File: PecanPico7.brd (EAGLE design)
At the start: 34.2 x 50 mm, 161 parts, among them IC1 Si4464-B1B-FM, IC10 TC1185-1.8VCT713, IC11 TC1185-2.5VCT713, IC12 ADR380ARTZ, IC13 RF6886, IC14 ALM-GP003, IC2 Si4464-B1B-FM, IC3 BME280_BME280, IC4 UBLOX_MAX-6, IC5 STM32F429IIH6, IC7 SPV1040, IC8 TXC_7Z, IC9 TPS62260DRVT, Q1 AP2301, Q2 AP2301, Q3 AP2301, U1 USD-SOCKETUSD, U2 PAC1720-1-AIA-TR, X1 CAMERA_HEADER

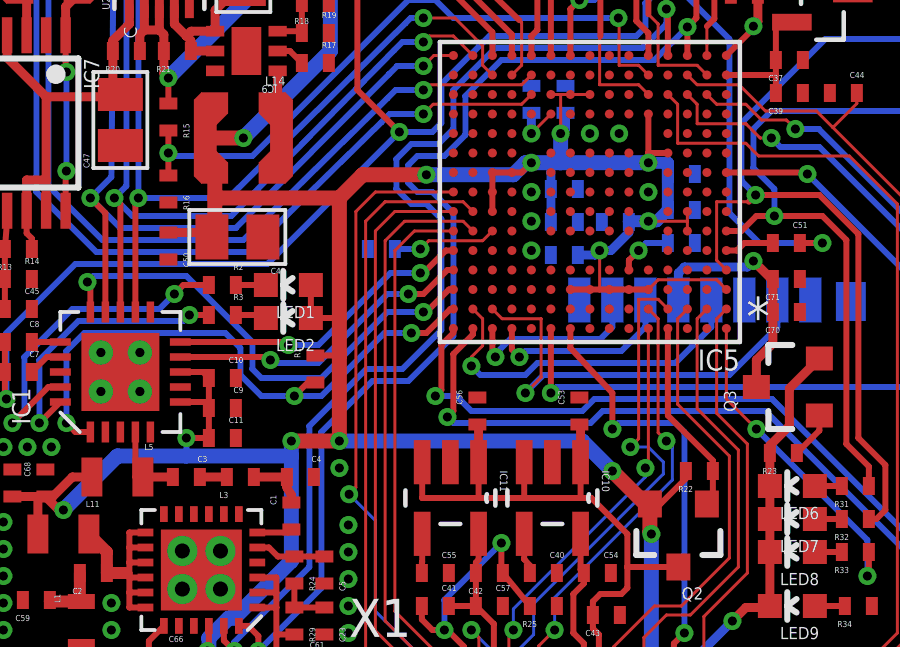
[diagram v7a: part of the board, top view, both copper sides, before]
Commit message: Moved parts around
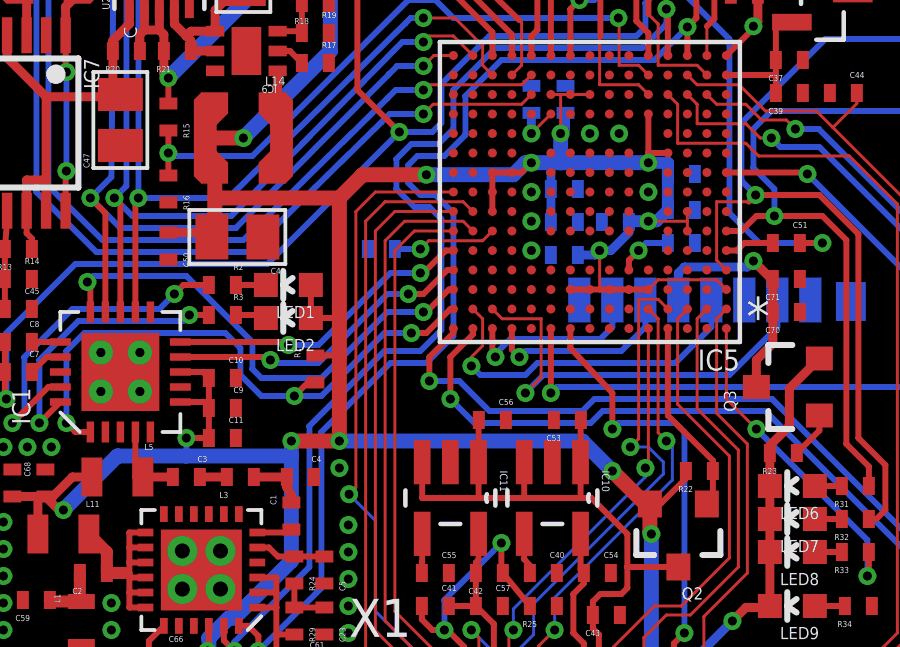
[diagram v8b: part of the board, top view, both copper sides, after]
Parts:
- moved C56 0.58 mm to (16.9, 14.5), turned to 180 degrees
- moved C53 0.50 mm to (19.4, 14.5), turned to 0 degrees
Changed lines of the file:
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@@
 </element>
 <element name="C40" library="PecanPico6" package="0402" value="470pF" x="18.6" y="9.4" rot="R180"/>
-<element name="C53" library="PecanPico6" package="0402" value="1uF" x="19.8" y="14.8" rot="R270"/>
+<element name="C53" library="PecanPico6" package="0402" value="1uF" x="19.4" y="14.5"/>
 <element name="C54" library="PecanPico6" package="0402" value="1uF" x="20.4" y="9.4" rot="R180"/>
 <element name="IC11" library="stm32f42x" package="SOT95P290X145-5N" value="TC1185-2.5VCT713" x="15.5" y="11.9" rot="R270">
@@
 </element>
 <element name="C55" library="PecanPico6" package="0402" value="470pF" x="15" y="9.4" rot="R180"/>
-<element name="C56" library="PecanPico6" package="0402" value="1uF" x="16.4" y="14.8" rot="R270"/>
+<element name="C56" library="PecanPico6" package="0402" value="1uF" x="16.9" y="14.5" rot="R180"/>
 <element name="C57" library="PecanPico6" package="0402" value="1uF" x="16.8" y="8.3" rot="R180"/>
 <element name="BATT" library="stm32f42x" package="LP-443440" value="LP-443440" x="17.1" y="20.1" rot="MR0"/>
@@
 <wire x1="23.7" y1="29.85" x2="24.85" y2="29.775" width="0" layer="19" extent="1-1"/>
 <wire x1="22.7" y1="29.85" x2="23.7" y2="29.85" width="0" layer="19" extent="1-1"/>
-<wire x1="19.8" y1="15.25" x2="19.5" y2="19.5" width="0" layer="19" extent="1-1"/>
-<wire x1="18.9" y1="13.0938" x2="19.8" y2="15.25" width="0" layer="19" extent="1-1"/>
-<wire x1="16.4" y1="15.25" x2="18.9" y2="13.0938" width="0" layer="19" extent="1-1"/>
-<wire x1="15.5" y1="13.0938" x2="16.4" y2="15.25" width="0" layer="19" extent="1-1"/>
+<wire x1="18.95" y1="14.5" x2="19.5" y2="19.5" width="0" layer="19" extent="1-1"/>
+<wire x1="18.9" y1="13.0938" x2="18.95" y2="14.5" width="0" layer="19" extent="1-1"/>
+<wire x1="17.35" y1="14.5" x2="18.9" y2="13.0938" width="0" layer="19" extent="1-1"/>
+<wire x1="15.5" y1="13.0938" x2="17.35" y2="14.5" width="0" layer="19" extent="1-1"/>
 <wire x1="19.05" y1="9.4" x2="18.9" y2="13.0938" width="0" layer="19" extent="1-1"/>
 <wire x1="19.05" y1="8.3" x2="19.05" y2="9.4" width="0" layer="19" extent="1-1"/>
@@
 <signal name="SWCLK">
 <contactref element="IC5" pad="A14"/>
-<via x="15.4" y="14.6" extent="1-16" drill="0.3"/>
+<via x="15.5" y="15.2" extent="1-16" drill="0.3"/>
 <wire x1="20.575" y1="14.8" x2="26" y2="14.8" width="0.2" layer="16"/>
 <wire x1="30.9" y1="9.9" x2="30.9" y2="5.84" width="0.2" layer="16"/>
-<wire x1="15.4" y1="14.6" x2="15.6" y2="14.4" width="0.2" layer="16"/>
-<wire x1="15.6" y1="14.4" x2="20.175" y2="14.4" width="0.2" layer="16"/>
+<wire x1="15.5" y1="15.2" x2="16.3" y2="14.4" width="0.2" layer="16"/>
+<wire x1="16.3" y1="14.4" x2="20.175" y2="14.4" width="0.2" layer="16"/>
 <wire x1="16.25" y1="17.55" x2="16.25" y2="17.35" width="0.2" layer="1"/>
-<wire x1="16.25" y1="17.35" x2="15.6" y2="16.7" width="0.2" layer="1"/>
-<wire x1="15.6" y1="16.7" x2="15.6" y2="14.8" width="0.2" layer="1"/>
-<wire x1="15.6" y1="14.8" x2="15.4" y2="14.6" width="0.2" layer="1"/>
+<wire x1="16.25" y1="17.35" x2="15.5" y2="16.6" width="0.2" layer="1"/>
+<wire x1="15.5" y1="16.6" x2="15.5" y2="15.2" width="0.2" layer="1"/>
 <wire x1="20.575" y1="14.8" x2="20.175" y2="14.4" width="0.2" layer="16"/>
 <contactref element="JP3" pad="2"/>
@@
 <signal name="SWDIO">
 <contactref element="IC5" pad="A15"/>
-<via x="15" y="15.3" extent="1-16" drill="0.3"/>
+<via x="14.8" y="15.8" extent="1-16" drill="0.3"/>
 <wire x1="20.3" y1="15.2" x2="26.22" y2="15.2" width="0.2" layer="16"/>
 <wire x1="19.9" y1="14.8" x2="20.3" y2="15.2" width="0.2" layer="16"/>
-<wire x1="15" y1="15.3" x2="15.7" y2="15.3" width="0.2" layer="16"/>
-<wire x1="15.7" y1="15.3" x2="16.2" y2="14.8" width="0.2" layer="16"/>
-<wire x1="16.2" y1="14.8" x2="19.9" y2="14.8" width="0.2" layer="16"/>
+<wire x1="14.8" y1="15.8" x2="15.8" y2="15.8" width="0.2" layer="16"/>
+<wire x1="15.8" y1="15.8" x2="16.8" y2="14.8" width="0.2" layer="16"/>
+<wire x1="16.8" y1="14.8" x2="19.9" y2="14.8" width="0.2" layer="16"/>
 <wire x1="15.6" y1="17.55" x2="15.6" y2="17.4" width="0.2" layer="1"/>
-<wire x1="15.6" y1="17.4" x2="15.2" y2="17" width="0.2" layer="1"/>
-<wire x1="15.2" y1="17" x2="15.2" y2="15.5" width="0.2" layer="1"/>
-<wire x1="15.2" y1="15.5" x2="15" y2="15.3" width="0.2" layer="1"/>
+<wire x1="15.6" y1="17.4" x2="14.8" y2="16.6" width="0.2" layer="1"/>
+<wire x1="14.8" y1="16.6" x2="14.8" y2="15.8" width="0.2" layer="1"/>
 <contactref element="JP3" pad="4"/>
 <wire x1="26.22" y1="15.2" x2="31.8" y2="9.6" width="0.2" layer="16"/>
@@
 <wire x1="8.3" y1="7.1" x2="10.8" y2="9.6" width="0.2" layer="16"/>
 <wire x1="10.8" y1="9.6" x2="10.8" y2="14.3" width="0.2" layer="16"/>
-<wire x1="10.8" y1="14.3" x2="12.7" y2="16.2" width="0.2" layer="16"/>
-<wire x1="12.7" y1="16.2" x2="13.9" y2="16.2" width="0.2" layer="16"/>
+<wire x1="10.8" y1="14.3" x2="13.3" y2="16.8" width="0.2" layer="16"/>
+<wire x1="13.3" y1="16.8" x2="14.5" y2="16.8" width="0.2" layer="16"/>
 <via x="22.7" y="28.2" extent="1-16" drill="0.3"/>
 <contactref element="IC5" pad="R4"/>
@@
 <wire x1="14.2" y1="23.7" x2="13.7" y2="23.2" width="0.2" layer="16"/>
 <wire x1="13.7" y1="23.2" x2="13.7" y2="22.2" width="0.2" layer="16"/>
-<wire x1="13.7" y1="22.2" x2="14.2" y2="21.7" width="0.2" layer="16"/>
-<wire x1="14.2" y1="21.7" x2="14.7" y2="21.7" width="0.2" layer="16"/>
-<wire x1="14.7" y1="21.7" x2="15.2" y2="21.2" width="0.2" layer="16"/>
+<wire x1="13.7" y1="22.2" x2="14.3" y2="21.6" width="0.2" layer="16"/>
+<wire x1="14.3" y1="21.6" x2="14.8" y2="21.6" width="0.2" layer="16"/>
+<wire x1="14.8" y1="21.6" x2="15.2" y2="21.2" width="0.2" layer="16"/>
 <wire x1="15.2" y1="21.2" x2="15.2" y2="17.5" width="0.2" layer="16"/>
-<wire x1="15.2" y1="17.5" x2="13.9" y2="16.2" width="0.2" layer="16"/>
+<wire x1="15.2" y1="17.5" x2="14.5" y2="16.8" width="0.2" layer="16"/>
 <contactref element="C72" pad="P$2"/>
 <wire x1="22.7" y1="28.2" x2="22.7" y2="28.95" width="0.2" layer="1"/>
@@
 <wire x1="9.1" y1="6.8" x2="11.2" y2="8.9" width="0.2" layer="16"/>
 <wire x1="11.2" y1="8.9" x2="11.2" y2="14.1" width="0.2" layer="16"/>
-<wire x1="11.2" y1="14.1" x2="12.9" y2="15.8" width="0.2" layer="16"/>
+<wire x1="11.2" y1="14.1" x2="13.5" y2="16.4" width="0.2" layer="16"/>
 <wire x1="9.1" y1="7.3" x2="9.1" y2="6.8" width="0.2" layer="1"/>
-<wire x1="12.9" y1="15.8" x2="14.1" y2="15.8" width="0.2" layer="16"/>
+<wire x1="13.5" y1="16.4" x2="14.7" y2="16.4" width="0.2" layer="16"/>
 <via x="23.4" y="27.6" extent="1-16" drill="0.3"/>
 <contactref element="IC5" pad="R3"/>
@@
 <wire x1="14.4" y1="23.3" x2="14.1" y2="23" width="0.2" layer="16"/>
 <wire x1="14.1" y1="23" x2="14.1" y2="22.4" width="0.2" layer="16"/>
-<wire x1="14.1" y1="22.4" x2="14.4" y2="22.1" width="0.2" layer="16"/>
-<wire x1="14.4" y1="22.1" x2="14.9" y2="22.1" width="0.2" layer="16"/>
-<wire x1="14.1" y1="15.8" x2="15.6" y2="17.3" width="0.2" layer="16"/>
+<wire x1="14.1" y1="22.4" x2="14.5" y2="22" width="0.2" layer="16"/>
+<wire x1="14.5" y1="22" x2="15" y2="22" width="0.2" layer="16"/>
+<wire x1="14.7" y1="16.4" x2="15.6" y2="17.3" width="0.2" layer="16"/>
 <wire x1="15.6" y1="17.3" x2="15.6" y2="21.4" width="0.2" layer="16"/>
-<wire x1="15.6" y1="21.4" x2="14.9" y2="22.1" width="0.2" layer="16"/>
+<wire x1="15.6" y1="21.4" x2="15" y2="22" width="0.2" layer="16"/>
 <contactref element="C73" pad="P$2"/>
 <wire x1="23.4" y1="27.6" x2="23.7" y2="27.9" width="0.2" layer="1"/>
@@
 <contactref element="C56" pad="P$2"/>
 <contactref element="IC11" pad="3"/>
-<wire x1="16.4398" y1="13.0938" x2="16.4398" y2="14.3102" width="0.3" layer="1"/>
-<wire x1="16.4398" y1="14.3102" x2="16.4" y2="14.35" width="0.3" layer="1"/>
-<wire x1="19.8398" y1="13.0938" x2="19.8398" y2="14.3102" width="0.3" layer="1"/>
-<wire x1="19.8398" y1="14.3102" x2="19.8" y2="14.35" width="0.3" layer="1"/>
 <contactref element="C43" pad="P$1"/>
 <contactref element="X1" pad="11"/>
@@
 <wire x1="20.45" y1="5.65" x2="20.45" y2="6.5" width="0.2" layer="1"/>
 <wire x1="23.1" y1="9.6" x2="21.4" y2="9.6" width="0.2" layer="1"/>
+<wire x1="16.4398" y1="13.0938" x2="16.4398" y2="14.5" width="0.2" layer="1"/>
+<wire x1="16.4398" y1="14.5" x2="16.45" y2="14.5" width="0.2" layer="1"/>
+<wire x1="19.8398" y1="13.0938" x2="19.8398" y2="14.4898" width="0.2" layer="1"/>
+<wire x1="19.8398" y1="14.4898" x2="19.85" y2="14.5" width="0.2" layer="1" curve="-90"/>
 </signal>
 <signal name="CAM_OFF">
